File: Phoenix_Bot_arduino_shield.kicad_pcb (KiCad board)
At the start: 2 copper layers, 102.9 x 54.6 mm, 0 parts

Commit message: Finished schematic and laid out PCB design
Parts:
- added J1: Analog_signal_male, Pin_Headers:Pin_Header_Straight_1x08_Pitch2.54mm, F.Cu at (121.9, 100.3)
- added J10: Ground, Pin_Headers:Pin_Header_Straight_1x06_Pitch2.54mm, F.Cu at (139.7, 87.6)
- added J11: Ground, Pin_Headers:Pin_Header_Straight_1x06_Pitch2.54mm, F.Cu at (161.3, 87.6)
- added J12: Ground, Pin_Headers:Pin_Header_Straight_1x08_Pitch2.54mm, F.Cu at (132.1, 77.5)
- added J14: PWN(10-5), Pin_Headers:Pin_Header_Straight_1x08_Pitch2.54mm, F.Cu at (146.1, 64.8)
- added J15: On Board Supply, Pin_Headers:Pin_Header_Straight_1x08_Pitch2.54mm, F.Cu at (139.7, 124.5)
- added J16: 1x8 Male, Pin_Headers:Pin_Header_Straight_1x08_Pitch2.54mm, F.Cu at (143.5, 111.8)
- added J17: 1x8 Male, Pin_Headers:Pin_Header_Straight_1x08_Pitch2.54mm, F.Cu at (143.5, 102.9)
- added J18: PWM_(6-1), Pin_Headers:Pin_Header_Straight_1x08_Pitch2.54mm, F.Cu at (170.2, 64.8)
- added J19: Analog_Pin_1, Pin_Headers:Pin_Header_Straight_1x08_Pitch2.54mm, F.Cu at (162.6, 124.5)
- added J2: Encoder_signal, Pin_Headers:Pin_Header_Straight_1x06_Pitch2.54mm, F.Cu at (161.3, 77.5)
- added J20: 1x8 Female, Pin_Headers:Pin_Header_Straight_1x08_Pitch2.54mm, F.Cu at (171.4, 102.9)
- added J21: 1x8 Female, Pin_Headers:Pin_Header_Straight_1x08_Pitch2.54mm, F.Cu at (171.4, 113.0)
- added J22: Serial, Pin_Headers:Pin_Header_Straight_1x08_Pitch2.54mm, F.Cu at (194.3, 64.8)
- added J23: ICSP, Pin_Headers:Pin_Header_Straight_2x03_Pitch2.54mm, F.Cu at (190.5, 77.5)
- added J24: Analog_Pin_2, Pin_Headers:Pin_Header_Straight_1x08_Pitch2.54mm, F.Cu at (186.7, 124.5)
- added J25: Digital_Pins, Pin_Headers:Pin_Header_Straight_2x18_Pitch2.54mm, F.Cu at (203.2, 68.6)
- added J27: Solenoid_terminal, Connectors_Terminal_Blocks:TerminalBlock_Altech_AK300-4_P5.00mm, F.Cu at (241.3, 66.0)
- added J28: Solendoid_middle_terminal, Connectors_Terminal_Blocks:TerminalBlock_Altech_AK300-4_P5.00mm, F.Cu at (241.3, 87.6)
- added J29: bottom_solenoid_terminal, Connectors_Terminal_Blocks:TerminalBlock_Altech_AK300-4_P5.00mm, F.Cu at (241.3, 109.2)
- added J3: Servo_signal, Pin_Headers:Pin_Header_Straight_1x06_Pitch2.54mm, F.Cu at (139.7, 77.5)
- added J4: Analog_signal_female, Pin_Headers:Pin_Header_Straight_1x08_Pitch2.54mm, F.Cu at (121.9, 77.5)
- added J5: Analog_signal_power, Pin_Headers:Pin_Header_Straight_1x08_Pitch2.54mm, F.Cu at (127.0, 100.3)
- added J6: Servo_Power, Pin_Headers:Pin_Header_Straight_1x06_Pitch2.54mm, F.Cu at (139.7, 82.5)
- added J7: Encoder_Power, Pin_Headers:Pin_Header_Straight_1x06_Pitch2.54mm, F.Cu at (161.3, 82.5)
- added J8: Analog_Power_female, Pin_Headers:Pin_Header_Straight_1x08_Pitch2.54mm, F.Cu at (127.0, 77.5)
- added J9: Ground, Pin_Headers:Pin_Header_Straight_1x08_Pitch2.54mm, F.Cu at (132.1, 100.3)
- added q1: solenoid_1, TO_SOT_Packages_THT:TO-220-3_Vertical, F.Cu at (222.2, 85.1)
- added q2: solenoid_4, TO_SOT_Packages_THT:TO-220-3_Vertical, F.Cu at (222.2, 73.7)
- added q3: solenoid_3, TO_SOT_Packages_THT:TO-220-3_Vertical, F.Cu at (222.2, 97.8)
- added q4: solenoid_5, TO_SOT_Packages_THT:TO-220-3_Vertical, F.Cu at (222.2, 121.9)
- added q5: solenoid_3, TO_SOT_Packages_THT:TO-220-3_Vertical, F.Cu at (222.2, 109.2)
- added q6: solenoid_6, TO_SOT_Packages_THT:TO-220-3_Vertical, F.Cu at (213.4, 73.7)
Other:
- board size 102.9 x 54.6 mm -> 135.9 x 64.8 mm

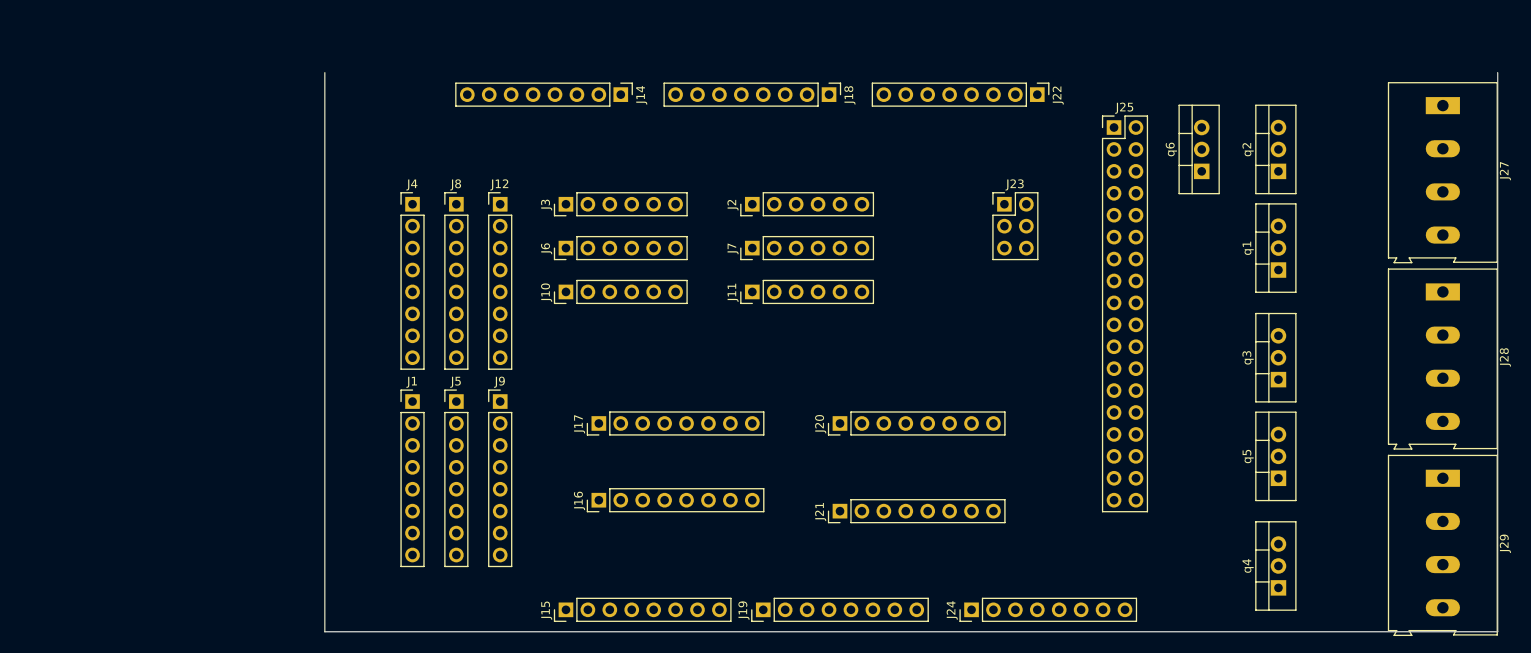
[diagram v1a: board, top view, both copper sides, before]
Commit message: Fixed hole alignment and pin count issues
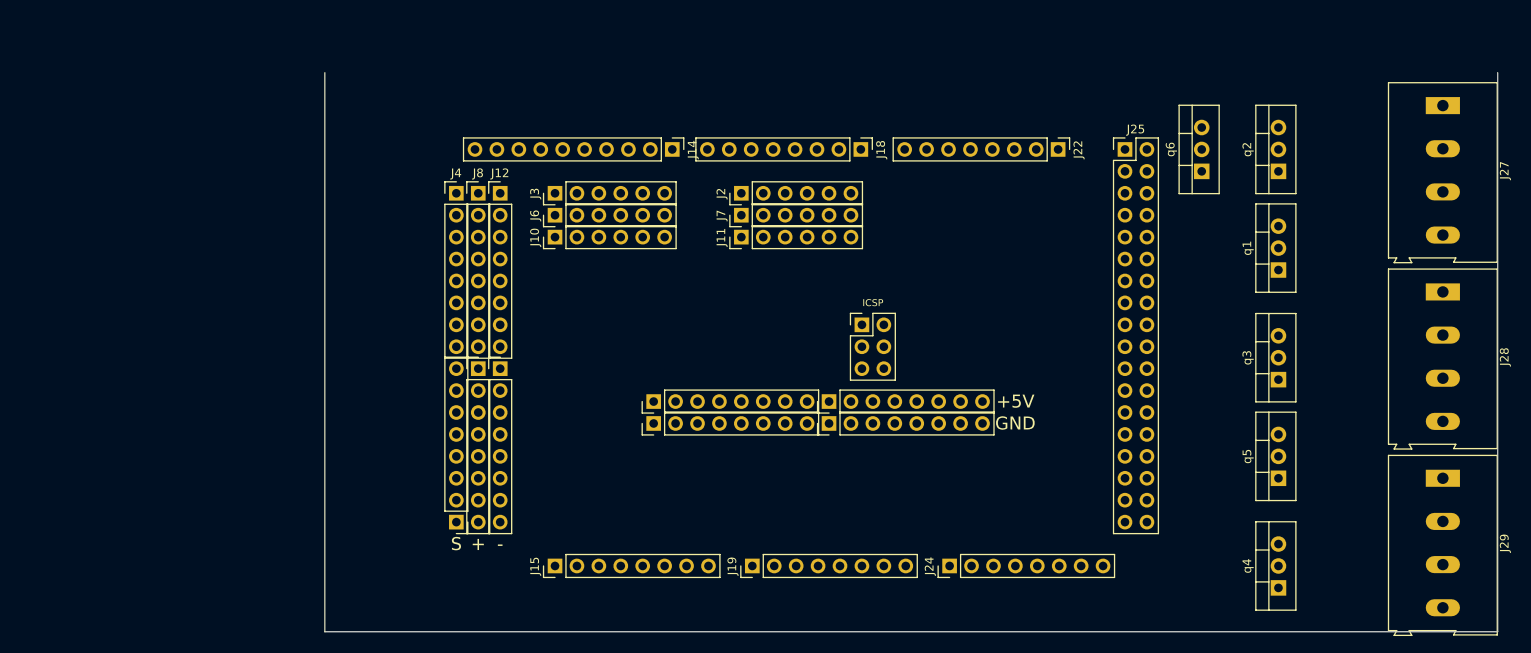
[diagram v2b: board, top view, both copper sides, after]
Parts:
- J14: footprint Pin_Headers:Pin_Header_Straight_1x08_Pitch2.54mm -> Pin_Headers:Pin_Header_Straight_1x10_Pitch2.54mm
- moved J23 21.6 mm to (174.0, 91.4)
- moved J1 14.9 mm to (127.0, 114.3), turned to 180 degrees
- moved J16 10.9 mm to (149.9, 102.9)
- moved J21 10.2 mm to (170.2, 102.9)
- moved J14 8.72 mm to (152.0, 71.1)
- moved J18 7.34 mm to (173.9, 71.1)
- moved J17 6.84 mm to (149.9, 100.3)
- moved J22 6.79 mm to (196.7, 71.1)
- moved J10 6.48 mm to (138.4, 81.3)
- moved J11 6.48 mm to (160.0, 81.3)
- moved J24 5.68 mm to (184.2, 119.4)
- moved J19 5.24 mm to (161.3, 119.4)
- moved J4 5.24 mm to (127.0, 76.2)
- moved J15 5.24 mm to (138.4, 119.4)
- moved J5 4.58 mm to (129.5, 96.5)
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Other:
- board text added: "+"
- board text added: "+5V"
- board text added: "-"
- board text added: "GND"
- board text added: "ICSP"
- board text added: "S"
